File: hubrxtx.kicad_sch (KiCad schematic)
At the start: 18 parts, among them J1 USB_B_Micro, U1 CH340K, U2 XC6206PxxxMR

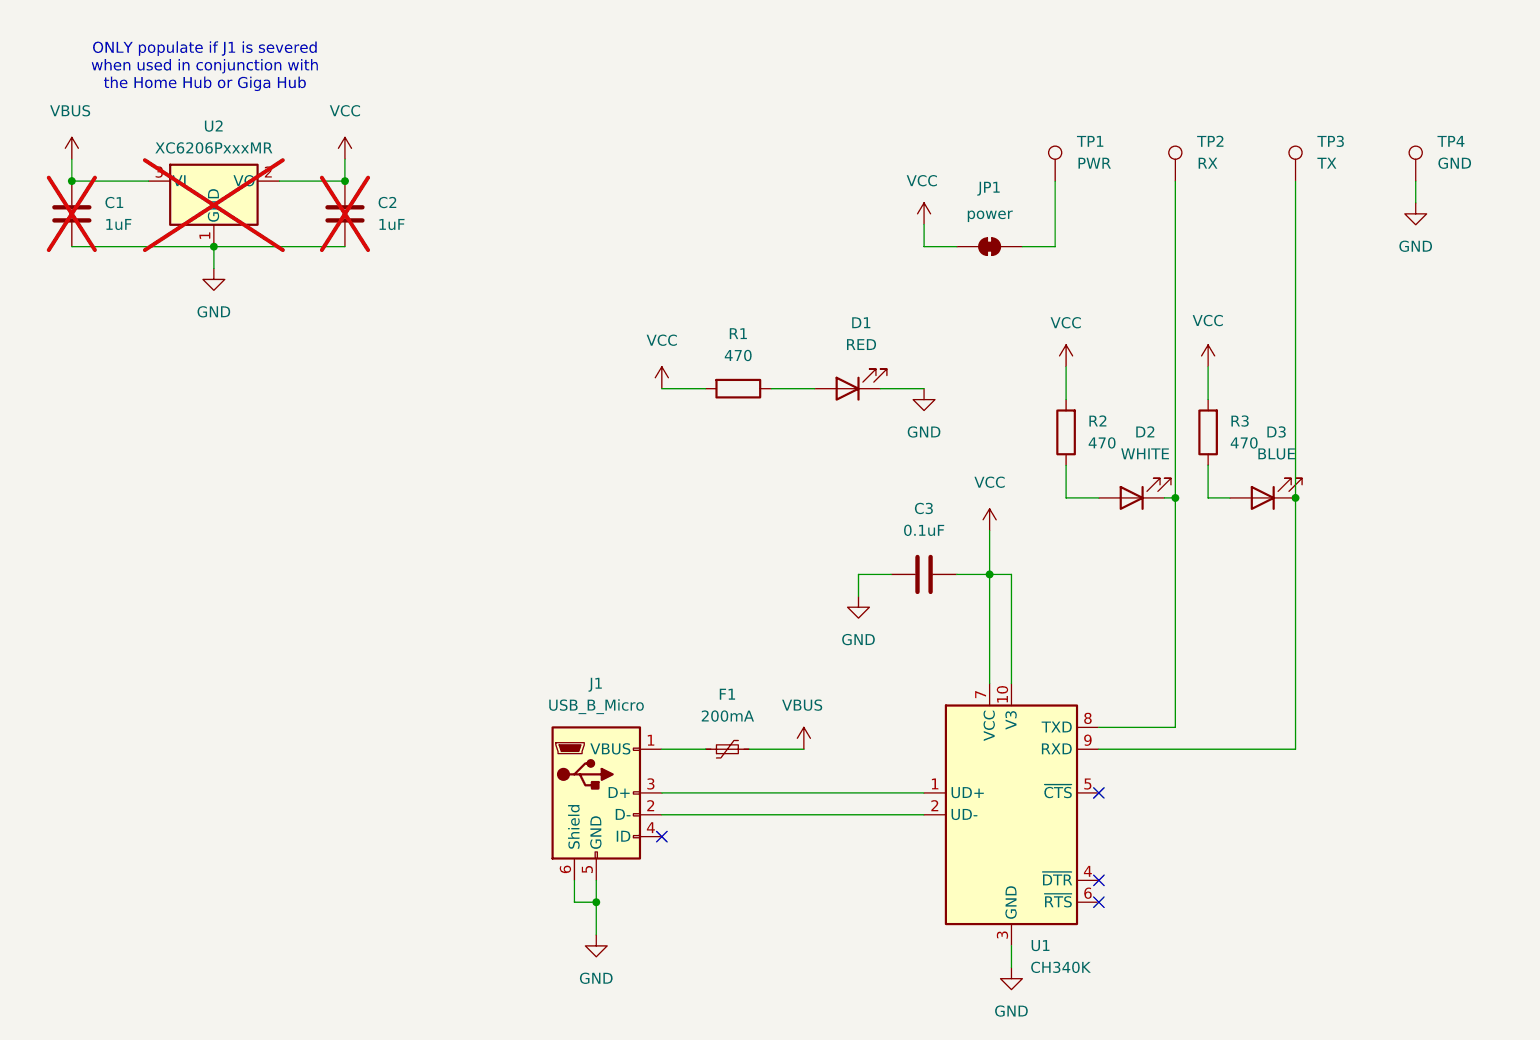
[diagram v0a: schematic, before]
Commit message: Update KiCad project
* Cleanup schematic
* Add net classes
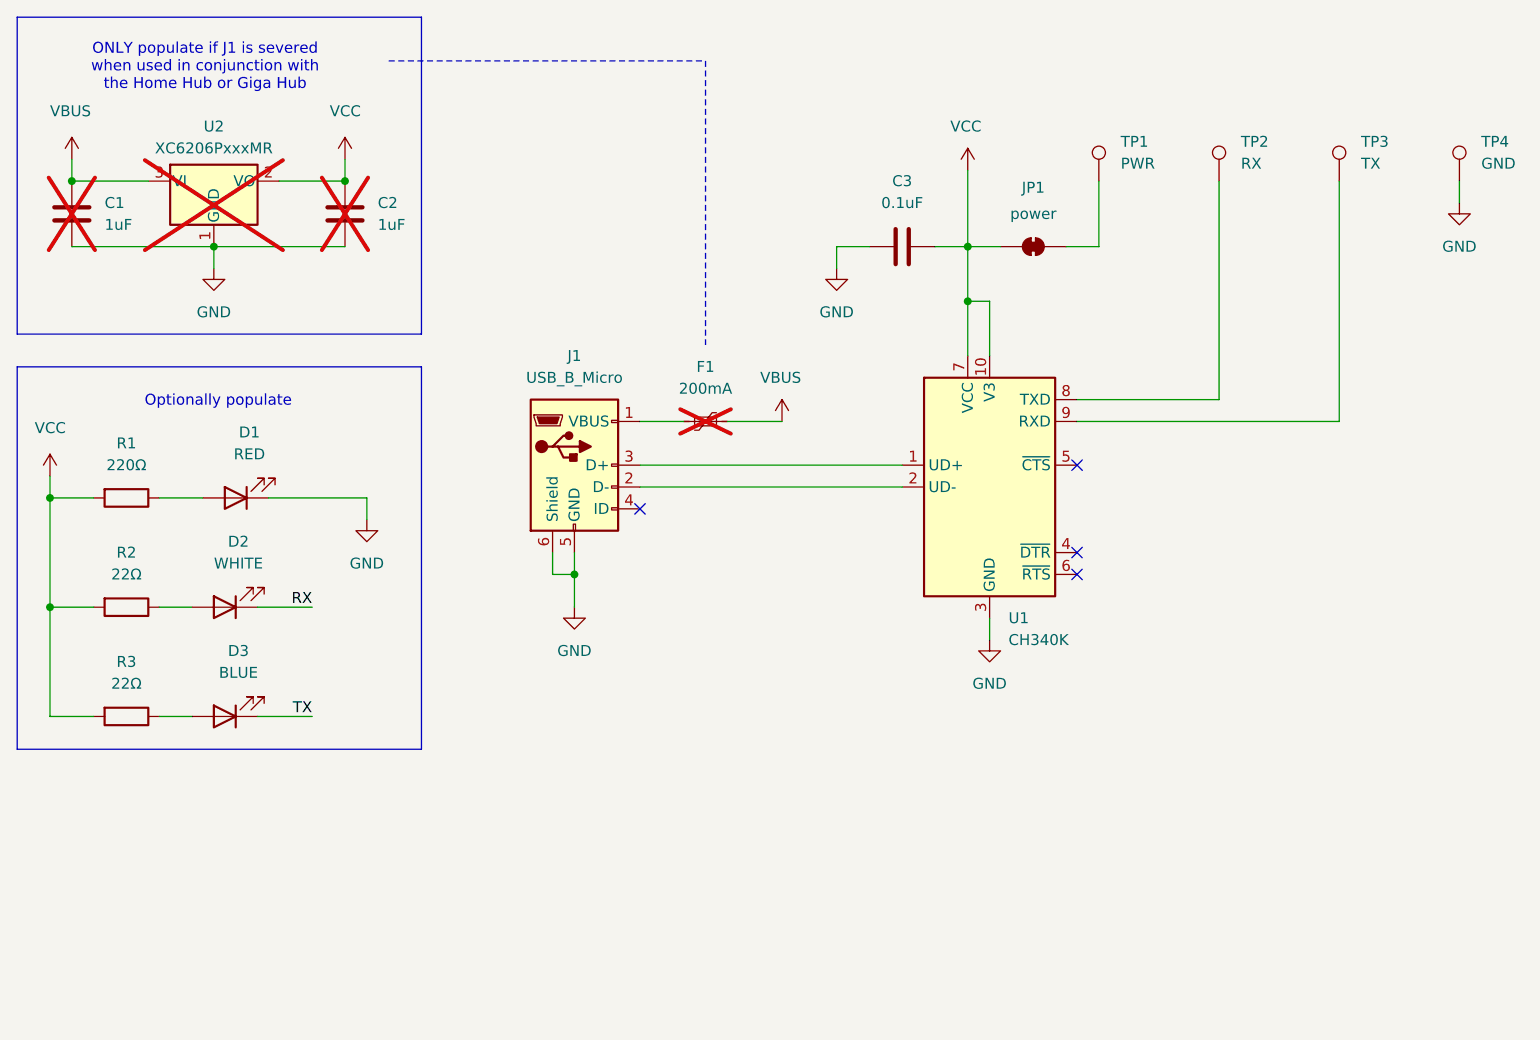
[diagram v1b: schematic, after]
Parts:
- F1: now not fitted
- R1: value 470 -> 220Ω
- R2, R3: value 470 -> 22Ω
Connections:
- net at TP2.1, U1.8 (TXD): no longer D2.1 (K)
- net at TP3.1, U1.9 (RXD): no longer D3.1 (K)
- new net RX: D2.1 (K)
- new net TX: D3.1 (K)
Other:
- note added: "Optionally populate"
- moved on the sheet: C3, D1, D2, D3, J1, JP1, R1, R2, R3, TP1, TP2, TP3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
